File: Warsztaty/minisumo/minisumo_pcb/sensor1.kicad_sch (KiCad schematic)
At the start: 7 parts, among them U5 VL53L0CXV0DH1

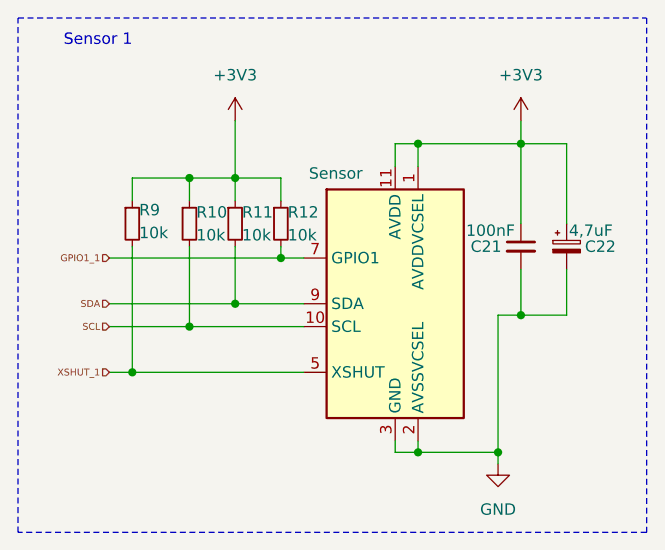
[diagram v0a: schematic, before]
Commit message: laczenie hierarchiczne schematu
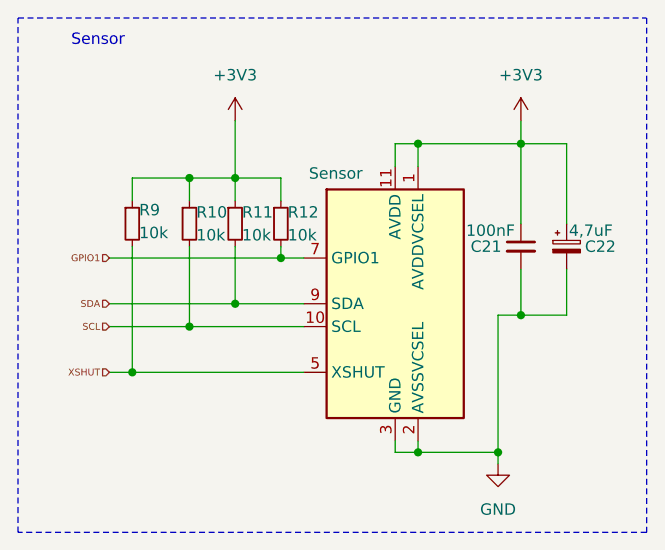
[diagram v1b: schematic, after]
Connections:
- net GPIO1_1 renamed GPIO1
- net XSHUT_1 renamed XSHUT
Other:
- note added: "Sensor"
- note removed: "Sensor 1"
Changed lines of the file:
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@@
 		)
 	)
-	(text "Sensor 1\n"
+	(text "Sensor\n"
 		(exclude_from_sim no)
 		(at 22.86 16.51 0)
@@
 		)
 	)
-	(hierarchical_label "XSHUT_1"
+	(hierarchical_label "XSHUT"
 		(shape input)
 		(at 24.13 53.34 180)
@@
 		)
 	)
-	(hierarchical_label "GPIO1_1"
+	(hierarchical_label "GPIO1"
 		(shape input)
 		(at 24.13 40.64 180)
@@
 					(unit 1)
 				)
+				(path "/7b99a4ad-c15f-48f5-acdf-b2b295c8ee3b/59b0bb17-8e81-44d5-808a-81d9b31dde61"
+					(reference "R21")
+					(unit 1)
+				)
+				(path "/7b99a4ad-c15f-48f5-acdf-b2b295c8ee3b/e2e15633-8dde-4add-b1e0-ff449194304b"
+					(reference "R25")
+					(unit 1)
+				)
+				(path "/7b99a4ad-c15f-48f5-acdf-b2b295c8ee3b/f48fad68-5a7d-4ca2-b957-317f1b6f3632"
+					(reference "R29")
+					(unit 1)
+				)
 			)
 		)
@@
 					(unit 1)
 				)
+				(path "/7b99a4ad-c15f-48f5-acdf-b2b295c8ee3b/59b0bb17-8e81-44d5-808a-81d9b31dde61"
+					(reference "#PWR029")
+					(unit 1)
+				)
+				(path "/7b99a4ad-c15f-48f5-acdf-b2b295c8ee3b/e2e15633-8dde-4add-b1e0-ff449194304b"
+					(reference "#PWR032")
+					(unit 1)
+				)
+				(path "/7b99a4ad-c15f-48f5-acdf-b2b295c8ee3b/f48fad68-5a7d-4ca2-b957-317f1b6f3632"
+					(reference "#PWR038")
+					(unit 1)
+				)
 			)
 		)
@@
 				(path "/7b99a4ad-c15f-48f5-acdf-b2b295c8ee3b/be05ae0d-f68b-4925-8f0e-be2ec3f0af2e"
 					(reference "U5")
+					(unit 1)
+				)
+				(path "/7b99a4ad-c15f-48f5-acdf-b2b295c8ee3b/59b0bb17-8e81-44d5-808a-81d9b31dde61"
+					(reference "U3")
+					(unit 1)
+				)
+				(path "/7b99a4ad-c15f-48f5-acdf-b2b295c8ee3b/e2e15633-8dde-4add-b1e0-ff449194304b"
+					(reference "U6")
+					(unit 1)
+				)
+				(path "/7b99a4ad-c15f-48f5-acdf-b2b295c8ee3b/f48fad68-5a7d-4ca2-b957-317f1b6f3632"
+					(reference "U12")
 					(unit 1)
 				)
@@
 					(unit 1)
 				)
+				(path "/7b99a4ad-c15f-48f5-acdf-b2b295c8ee3b/59b0bb17-8e81-44d5-808a-81d9b31dde61"
+					(reference "#PWR030")
+					(unit 1)
+				)
+				(path "/7b99a4ad-c15f-48f5-acdf-b2b295c8ee3b/e2e15633-8dde-4add-b1e0-ff449194304b"
+					(reference "#PWR033")
+					(unit 1)
+				)
+				(path "/7b99a4ad-c15f-48f5-acdf-b2b295c8ee3b/f48fad68-5a7d-4ca2-b957-317f1b6f3632"
+					(reference "#PWR039")
+					(unit 1)
+				)
 			)
 		)
@@
 					(unit 1)
 				)
+				(path "/7b99a4ad-c15f-48f5-acdf-b2b295c8ee3b/59b0bb17-8e81-44d5-808a-81d9b31dde61"
+					(reference "R23")
+					(unit 1)
+				)
+				(path "/7b99a4ad-c15f-48f5-acdf-b2b295c8ee3b/e2e15633-8dde-4add-b1e0-ff449194304b"
+					(reference "R27")
+					(unit 1)
+				)
+				(path "/7b99a4ad-c15f-48f5-acdf-b2b295c8ee3b/f48fad68-5a7d-4ca2-b957-317f1b6f3632"
+					(reference "R31")
+					(unit 1)
+				)
 			)
 		)
@@
 					(unit 1)
 				)
+				(path "/7b99a4ad-c15f-48f5-acdf-b2b295c8ee3b/59b0bb17-8e81-44d5-808a-81d9b31dde61"
+					(reference "R22")
+					(unit 1)
+				)
+				(path "/7b99a4ad-c15f-48f5-acdf-b2b295c8ee3b/e2e15633-8dde-4add-b1e0-ff449194304b"
+					(reference "R26")
+					(unit 1)
+				)
+				(path "/7b99a4ad-c15f-48f5-acdf-b2b295c8ee3b/f48fad68-5a7d-4ca2-b957-317f1b6f3632"
+					(reference "R30")
+					(unit 1)
+				)
 			)
 		)
@@
 				(path "/7b99a4ad-c15f-48f5-acdf-b2b295c8ee3b/be05ae0d-f68b-4925-8f0e-be2ec3f0af2e"
 					(reference "C22")
+					(unit 1)
+				)
+				(path "/7b99a4ad-c15f-48f5-acdf-b2b295c8ee3b/59b0bb17-8e81-44d5-808a-81d9b31dde61"
+					(reference "C13")
+					(unit 1)
+				)
+				(path "/7b99a4ad-c15f-48f5-acdf-b2b295c8ee3b/e2e15633-8dde-4add-b1e0-ff449194304b"
+					(reference "C15")
+					(unit 1)
+				)
+				(path "/7b99a4ad-c15f-48f5-acdf-b2b295c8ee3b/f48fad68-5a7d-4ca2-b957-317f1b6f3632"
+					(reference "C17")
 					(unit 1)
 				)
@@
 					(unit 1)
 				)
+				(path "/7b99a4ad-c15f-48f5-acdf-b2b295c8ee3b/59b0bb17-8e81-44d5-808a-81d9b31dde61"
+					(reference "#PWR028")
+					(unit 1)
+				)
+				(path "/7b99a4ad-c15f-48f5-acdf-b2b295c8ee3b/e2e15633-8dde-4add-b1e0-ff449194304b"
+					(reference "#PWR031")
+					(unit 1)
+				)
+				(path "/7b99a4ad-c15f-48f5-acdf-b2b295c8ee3b/f48fad68-5a7d-4ca2-b957-317f1b6f3632"
+					(reference "#PWR034")
+					(unit 1)
+				)
 			)
 		)
@@
 					(unit 1)
 				)
+				(path "/7b99a4ad-c15f-48f5-acdf-b2b295c8ee3b/59b0bb17-8e81-44d5-808a-81d9b31dde61"
+					(reference "R24")
+					(unit 1)
+				)
+				(path "/7b99a4ad-c15f-48f5-acdf-b2b295c8ee3b/e2e15633-8dde-4add-b1e0-ff449194304b"
+					(reference "R28")
+					(unit 1)
+				)
+				(path "/7b99a4ad-c15f-48f5-acdf-b2b295c8ee3b/f48fad68-5a7d-4ca2-b957-317f1b6f3632"
+					(reference "R32")
+					(unit 1)
+				)
 			)
 		)
@@
 					(unit 1)
 				)
+				(path "/7b99a4ad-c15f-48f5-acdf-b2b295c8ee3b/59b0bb17-8e81-44d5-808a-81d9b31dde61"
+					(reference "C8")
+					(unit 1)
+				)
+				(path "/7b99a4ad-c15f-48f5-acdf-b2b295c8ee3b/e2e15633-8dde-4add-b1e0-ff449194304b"
+					(reference "C14")
+					(unit 1)
+				)
+				(path "/7b99a4ad-c15f-48f5-acdf-b2b295c8ee3b/f48fad68-5a7d-4ca2-b957-317f1b6f3632"
+					(reference "C16")
+					(unit 1)
+				)

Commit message: chyba gotowy schemat
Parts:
- C21, C22: footprint (none) -> Capacitor_SMD:C_0805_2012Metric_Pad1.18x1.45mm_HandSolder
- R10, R11, R12, R9: footprint (none) -> Resistor_SMD:R_0805_2012Metric_Pad1.20x1.40mm_HandSolder
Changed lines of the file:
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@@
 			)
 		)
-		(property "Footprint" ""
+		(property "Footprint" "Resistor_SMD:R_0805_2012Metric_Pad1.20x1.40mm_HandSolder"
 			(at 26.67 36.83 0)
 			(effects
@@
 			)
 		)
-		(property "Footprint" ""
+		(property "Footprint" "Resistor_SMD:R_0805_2012Metric_Pad1.20x1.40mm_HandSolder"
 			(at 38.1 36.83 0)
 			(effects
@@
 			)
 		)
-		(property "Footprint" ""
+		(property "Footprint" "Resistor_SMD:R_0805_2012Metric_Pad1.20x1.40mm_HandSolder"
 			(at 33.02 36.83 0)
 			(effects
@@
 			)
 		)
-		(property "Footprint" ""
+		(property "Footprint" "Capacitor_SMD:C_0805_2012Metric_Pad1.18x1.45mm_HandSolder"
 			(at 74.93 39.37 0)
 			(effects
@@
 			)
 		)
-		(property "Footprint" ""
+		(property "Footprint" "Resistor_SMD:R_0805_2012Metric_Pad1.20x1.40mm_HandSolder"
 			(at 43.18 36.83 0)
 			(effects
@@
 			)
 		)
-		(property "Footprint" ""
+		(property "Footprint" "Capacitor_SMD:C_0805_2012Metric_Pad1.18x1.45mm_HandSolder"
 			(at 69.85 39.37 0)
 			(effects

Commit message: chyba gotowy schemat
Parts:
- removed C21: 100nF, Capacitor_SMD:C_0805_2012Metric_Pad1.18x1.45mm_HandSolder, symbol Device:C_Small
- removed C22: 4,7uF, Capacitor_SMD:C_0805_2012Metric_Pad1.18x1.45mm_HandSolder, symbol Device:C_Polarized_Small
- removed R10, R11, R12, R9: 10k, Resistor_SMD:R_0805_2012Metric_Pad1.20x1.40mm_HandSolder, symbol Device:R_Small
- removed U5: VL53L0CXV0DH1, Sensor_Distance:ST_VL53L1x, symbol Sensor_Distance:VL53L0CXV0DH1
- added SPI2: MTSW-103-23-F-D-230, MTSW-103-23-F-D-230:SAMTEC_MTSW-103-23-F-D-230, symbol MTSW-103-23-F-D-230:MTSW-103-23-F-D-230
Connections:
- net GND: now also SPI2.01
- net SCL: now also SPI2.04
- net SDA: now also SPI2.03
- new net +5V: SPI2.02
- new net G1: SPI2.06
- new net X1: SPI2.05
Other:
- note added: "Sensor1"
- note removed: "Sensor"

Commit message: stan przed usunięciem jednego czujnika lini
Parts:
- added R1: 10k, Resistor_SMD:R_0805_2012Metric, symbol Device:R_Small
- added R2: 20k, Resistor_SMD:R_0805_2012Metric, symbol Device:R_Small
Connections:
- net GND: now also R2.1
- net X1: now also R1.2, R2.2; no longer SPI2.05
- new net: R1.1, SPI2.05

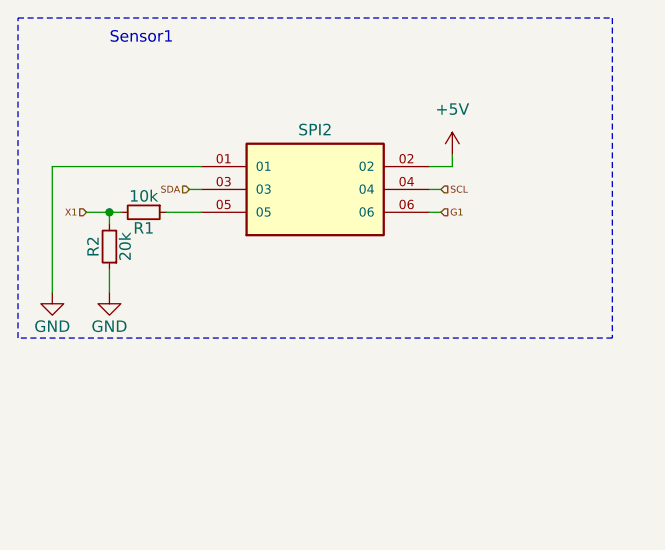
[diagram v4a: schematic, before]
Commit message: Wstępny wyglad robota i płytki
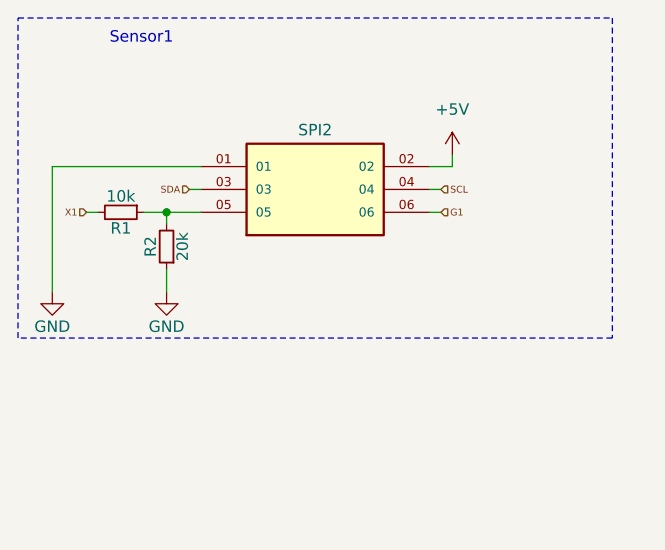
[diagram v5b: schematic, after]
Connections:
- net X1: no longer R2.2
- net at R1.1, SPI2.05: now also R2.2
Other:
- moved on the sheet: R1, R2
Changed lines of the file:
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@@
 	(paper "A4")
 	(junction
-		(at 24.13 35.56)
+		(at 30.48 35.56)
 		(diameter 0)
 		(color 0 0 0 0)
@@
 	(wire
 		(pts
+			(xy 30.48 35.56) (xy 34.29 35.56)
+		)
+		(stroke
+			(width 0)
+			(type default)
+		)
+	)
+	(wire
+		(pts
 			(xy 59.69 33.02) (xy 60.96 33.02)
 		)
@@
 	(wire
 		(pts
-			(xy 21.59 35.56) (xy 24.13 35.56)
-		)
-		(stroke
-			(width 0)
-			(type default)
-		)
-	)
-	(wire
-		(pts
-			(xy 24.13 41.91) (xy 24.13 44.45)
-		)
-		(stroke
-			(width 0)
-			(type default)
-		)
-	)
-	(wire
-		(pts
-			(xy 24.13 35.56) (xy 24.13 36.83)
-		)
-		(stroke
-			(width 0)
-			(type default)
-		)
-	)
-	(wire
-		(pts
-			(xy 24.13 35.56) (xy 25.4 35.56)
-		)
-		(stroke
-			(width 0)
-			(type default)
-		)
-	)
-	(wire
-		(pts
-			(xy 30.48 35.56) (xy 34.29 35.56)
+			(xy 30.48 41.91) (xy 30.48 44.45)
+		)
+		(stroke
+			(width 0)
+			(type default)
+		)
+	)
+	(wire
+		(pts
+			(xy 21.59 35.56) (xy 22.86 35.56)
+		)
+		(stroke
+			(width 0)
+			(type default)
+		)
+	)
+	(wire
+		(pts
+			(xy 27.94 35.56) (xy 30.48 35.56)
 		)
 		(stroke
@@
 		(pts
 			(xy 59.69 30.48) (xy 62.23 30.48)
+		)
+		(stroke
+			(width 0)
+			(type default)
+		)
+	)
+	(wire
+		(pts
+			(xy 30.48 35.56) (xy 30.48 36.83)
 		)
 		(stroke
@@
 	(symbol
 		(lib_id "Device:R_Small")
-		(at 27.94 35.56 270)
+		(at 25.4 35.56 270)
 		(unit 1)
 		(exclude_from_sim no)
@@
 		(dnp no)
 		(property "Reference" "R1"
-			(at 27.94 37.338 90)
+			(at 25.4 37.338 90)
 			(effects
 				(font
@@
 		)
 		(property "Value" "10k"
-			(at 27.94 33.782 90)
+			(at 25.4 33.782 90)
 			(effects
 				(font
@@
 		)
 		(property "Footprint" "Resistor_SMD:R_0805_2012Metric"
-			(at 27.94 35.56 0)
+			(at 25.4 35.56 0)
 			(effects
 				(font
@@
 		)
 		(property "Datasheet" "~"
-			(at 27.94 35.56 0)
+			(at 25.4 35.56 0)
 			(effects
 				(font
@@
 		)
 		(property "Description" "Resistor, small symbol"
-			(at 27.94 35.56 0)
+			(at 25.4 35.56 0)
 			(effects
 				(font
@@
 	(symbol
 		(lib_id "Device:R_Small")
-		(at 24.13 39.37 180)
+		(at 30.48 39.37 180)
 		(unit 1)
 		(exclude_from_sim no)
@@
 		(dnp no)
 		(property "Reference" "R2"
-			(at 22.352 39.37 90)
+			(at 28.702 39.37 90)
 			(effects
 				(font
@@
 		)
 		(property "Value" "20k"
-			(at 25.908 39.37 90)
+			(at 32.258 39.37 90)
 			(effects
 				(font
@@
 		)
 		(property "Footprint" "Resistor_SMD:R_0805_2012Metric"
-			(at 24.13 39.37 0)
+			(at 30.48 39.37 0)
 			(effects
 				(font
@@
 		)
 		(property "Datasheet" "~"
-			(at 24.13 39.37 0)
+			(at 30.48 39.37 0)
 			(effects
 				(font
@@
 		)
 		(property "Description" "Resistor, small symbol"
-			(at 24.13 39.37 0)
+			(at 30.48 39.37 0)
 			(effects
 				(font
@@
 	(symbol
 		(lib_id "power:GND")
-		(at 24.13 44.45 0)
+		(at 30.48 44.45 0)
 		(unit 1)
 		(exclude_from_sim no)
@@
 		(dnp no)
 		(property "Reference" "#PWR029"
-			(at 24.13 50.8 0)
+			(at 30.48 50.8 0)
 			(effects
 				(font
@@
 		)
 		(property "Value" "GND"
-			(at 24.13 48.26 0)
+			(at 30.48 48.26 0)
 			(effects
 				(font
@@
 		)
 		(property "Footprint" ""
-			(at 24.13 44.45 0)
+			(at 30.48 44.45 0)
 			(effects
 				(font
@@
 		)
 		(property "Datasheet" ""
-			(at 24.13 44.45 0)
+			(at 30.48 44.45 0)
 			(effects
 				(font
@@
 		)
 		(property "Description" "Power symbol creates a global label with name \"GND\" , ground"
-			(at 24.13 44.45 0)
-			(effects
-				(font
+			(at 30.48 44.45 0)
+			(effects
+				(font

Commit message: koncowy projekt plytki i chyba model tez
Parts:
- renumbered SPI2 to ES1
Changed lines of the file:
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@@
 		(on_board yes)
 		(dnp no)
-		(property "Reference" "SPI2"
+		(property "Reference" "ES1"
 			(at 46.99 26.416 0)
 			(effects
@@
 			(project "minisumo_pcb"
 				(path "/7b99a4ad-c15f-48f5-acdf-b2b295c8ee3b/430967e4-ab10-46f6-85c9-d4921e2b74f6"
-					(reference "SPI2")
+					(reference "ES1")
 					(unit 1)
 				)

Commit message: prawdopodobnie koncowa wersja płytki
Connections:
- net X1 renamed XSHUT_1
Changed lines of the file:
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@@
 		)
 	)
-	(hierarchical_label "X1"
+	(hierarchical_label "XSHUT_1"
 		(shape input)
 		(at 21.59 35.56 180)
